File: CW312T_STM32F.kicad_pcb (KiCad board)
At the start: 2 copper layers, 58.7 x 53.7 mm, 21 parts, among them J1 HDR_6_2.54, P1 PCIEx4 EDGE CONNECTOR, U1 STM32F100RBT6B

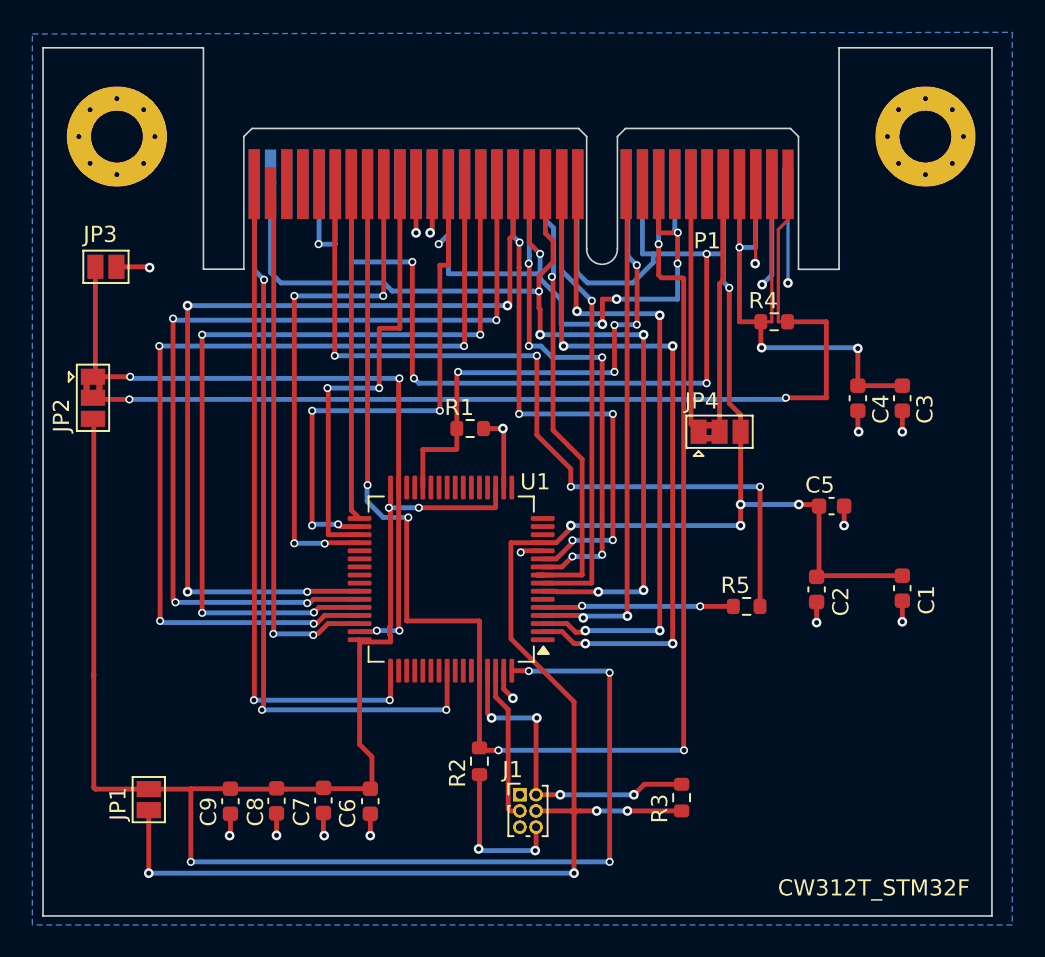
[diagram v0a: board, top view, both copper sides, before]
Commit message: updated CW312T-STM32F1 design
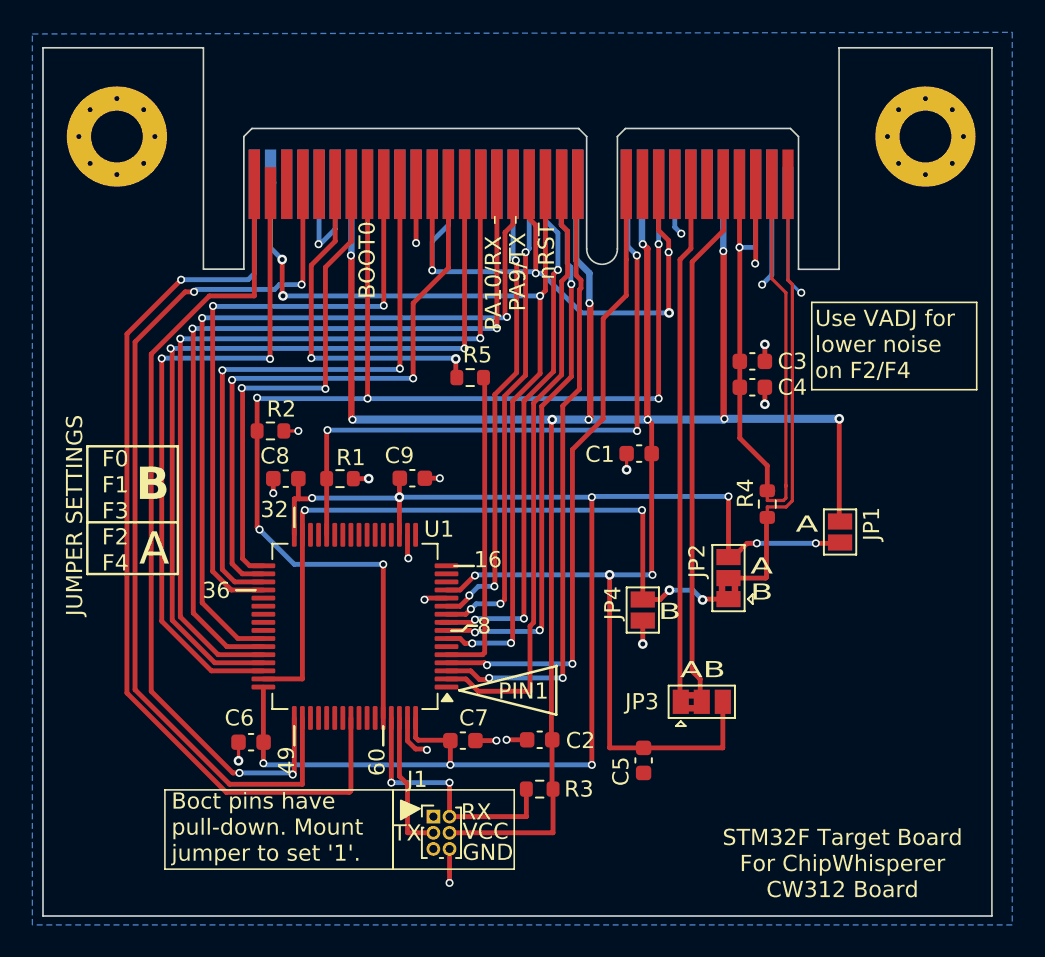
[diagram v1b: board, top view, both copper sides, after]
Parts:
- added PCB1: CE, Silkscrren_Symbols:CE-Logo_8.5x6mm_SilkScreen, F.Cu at (126.3, 97.2)
- added PCB2: WEEE, Silkscrren_Symbols:WEEE-Logo_8.4x12mm_SilkScreen, F.Cu at (124.2, 86.7)
- added PCB3: Pb_Free, Silkscrren_Symbols:Pb_Free_8.0x8.0mm_SilkScreen, F.Cu at (135.4, 97.4)
- moved JP1 45.8 mm to (160.6, 85.5), turned to 90 degrees
- moved JP2 40.9 mm to (153.7, 88.3), turned to 90 degrees
- moved JP4 39.4 mm to (148.3, 90.3), turned to 90 degrees
- moved R2 24.2 mm to (125.3, 79.2), turned to 0 degrees
- moved C9 22.9 mm to (134.1, 82.2), turned to 0 degrees
- moved R5 22.2 mm to (137.7, 76.0), turned to 0 degrees
- moved C8 19.9 mm to (126.3, 82.2), turned to 180 degrees
- moved C5 19.6 mm to (148.4, 99.6), turned to -90 degrees
- moved C2 19.5 mm to (142.0, 98.3), turned to 180 degrees
- moved C1 18.3 mm to (148.1, 80.7), turned to 180 degrees
- moved JP3 16.7 mm to (152.0, 96.0)
- moved R4 11.3 mm to (156.1, 83.8), turned to 90 degrees
- moved C3 9.55 mm to (155.1, 75.0), turned to 0 degrees
- moved C7 9.39 mm to (137.2, 98.4), turned to 0 degrees
- moved R3 8.79 mm to (142.0, 101.4), turned to 0 degrees
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- renumbered JP4 to JP3, JP3 to JP4
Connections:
- U1 pad 50: /TD1 -> /TDI
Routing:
- net /TDI: track 0.00 -> 56.4 mm, vias 0 -> 2
- net Net-(P1-SHUNTL): track 62.1 -> 28.1 mm, vias 2 -> 0
- net Net-(P1-CLKOUT): track 51.2 -> 21.5 mm, vias 4 -> 2
- net Net-(U1B-VDD_1): track 117.3 -> 91.3 mm, vias 6 -> 9
- net Net-(P1-FILTIN): track 15.4 -> 32.9 mm
- net Net-(P1-VCC1.2): track 15.5 -> 32.0 mm
- net GND: track 108.3 -> 93.3 mm, vias 27 -> 25
- net /BOOT0: track 90.8 -> 77.6 mm, vias 5 -> 6
- net /TRST: track 46.7 -> 58.1 mm, vias 3 -> 1
- net /FILT_HP: track 36.6 -> 46.6 mm, vias 3 -> 1
- net /CS: track 20.9 -> 30.6 mm, vias 0 -> 2
- net /MISO: track 28.1 -> 37.6 mm
- net /BOOT1: track 32.2 -> 41.1 mm, vias 5 -> 3
- net VCC: track 179.6 -> 171.1 mm
- net /TCK: track 42.2 -> 50.1 mm
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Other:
- board text added: "16"
- board text added: "32"
- board text added: "36"
- board text added: "49"
- board text added: "60"
- board text added: "8"
- board text added: "A"
- board text added: "A B"
- board text added: "AB"
- board text added: "B"
- board text added: "BOOT0"
- board text added: "BT0"
- board text added: "BT1"
- board text added: "Boct pins have pull-down. Mount jumper to set '1'."
- board text added: "F0 F1 F3 F2 F4"
- board text added: "GND"
- board text added: "JUMPER SETTINGS"
- board text added: "NewAE Technology Inc. NAE-CW312T-STM32F-01 RoHS / PB-Free"
- board text added: "PA10/RX"
- board text added: "PA9/TX"
- board text added: "PIN1"
- board text added: "RX"
- board text added: "STM32F Target Board For ChipWhisperer CW312 Board"
- board text added: "TX"
- board text added: "Use VADJ for lower noise on F2/F4"
- board text added: "VCC"
- board text added: "nRST"
- board text removed: "CW312T_STM32F"
